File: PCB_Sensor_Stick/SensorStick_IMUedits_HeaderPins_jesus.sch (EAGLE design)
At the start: 50 parts

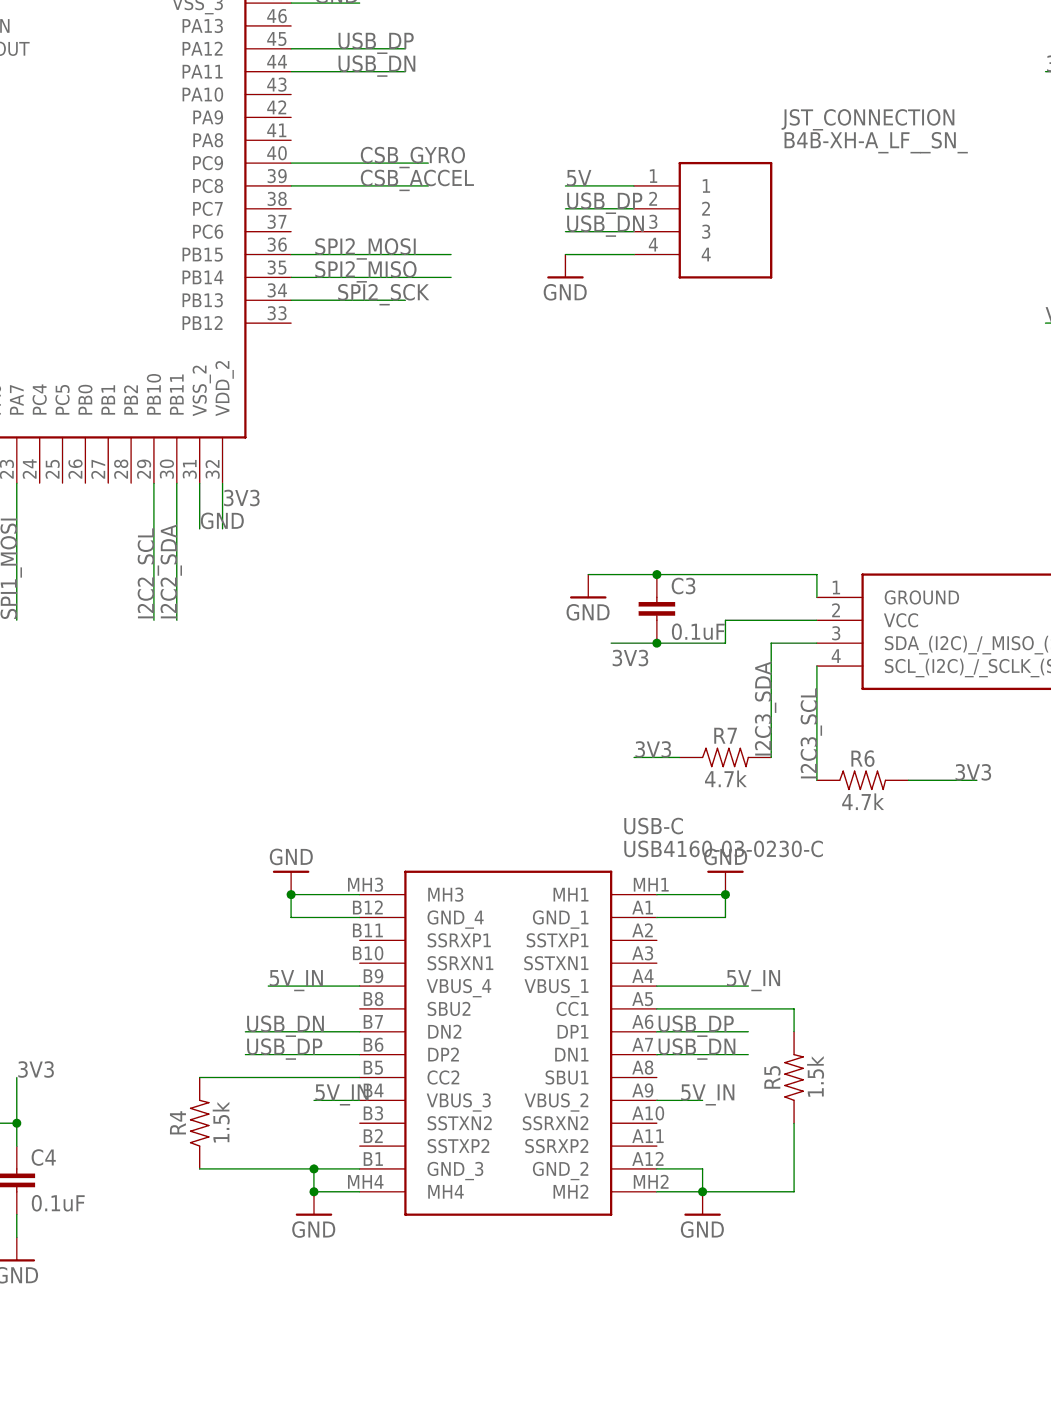
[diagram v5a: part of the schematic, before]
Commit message: J - Removed USB-C connector, wired JST-XH connector, PCB/Schematic first draft
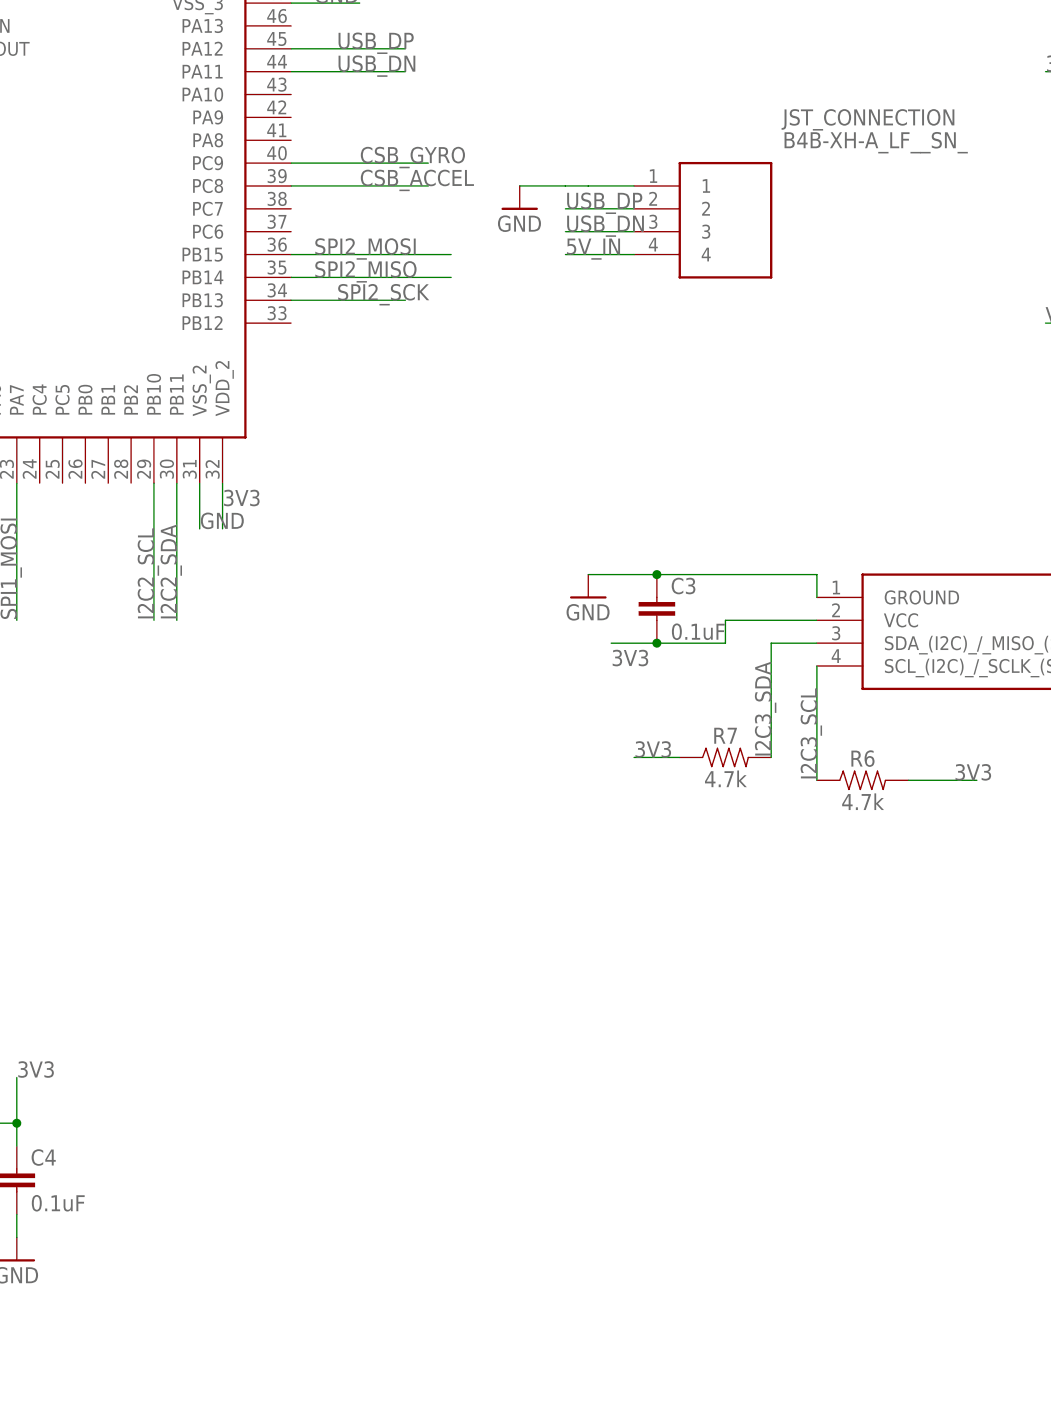
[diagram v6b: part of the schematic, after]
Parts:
- removed R4, R5: 1.5k, SparkFun-Resistors:1.5KOHM-0603-1/10W-1%
- removed USB-C: USB4160-03-0230-C, USB4160-03-0230-C:USB4160-03-0230-C
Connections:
- removed net N$10: R4.2, USB-C.CC2
- removed net N$3: R5.2, USB-C.CC1
- net 5V: no longer JST_CONNECTION.1
- net 5V_IN: now also JST_CONNECTION.4; no longer USB-C.VBUS_1, USB-C.VBUS_2, USB-C.VBUS_3, USB-C.VBUS_4
- net GND: now also JST_CONNECTION.1; no longer JST_CONNECTION.4, R4.1, R5.1, USB-C.GND_1, USB-C.GND_2, USB-C.GND_3, USB-C.GND_4, USB-C.MH1, USB-C.MH2, USB-C.MH3, USB-C.MH4
- net USB_DN: no longer USB-C.DN1, USB-C.DN2
- net USB_DP: no longer USB-C.DP1, USB-C.DP2
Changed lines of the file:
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@@
 <part name="C13" library="SparkFun-Capacitors" deviceset="0.22UF" device="-0603-25V-10%" value="0.22uF"/>
 <part name="GND14" library="supply1" library_urn="urn:adsk.eagle:library:371" deviceset="GND" device=""/>
-<part name="USB-C" library="USB4160-03-0230-C" deviceset="USB4160-03-0230-C" device=""/>
-<part name="GND15" library="supply1" library_urn="urn:adsk.eagle:library:371" deviceset="GND" device=""/>
-<part name="GND16" library="supply1" library_urn="urn:adsk.eagle:library:371" deviceset="GND" device=""/>
-<part name="GND17" library="supply1" library_urn="urn:adsk.eagle:library:371" deviceset="GND" device=""/>
-<part name="GND18" library="supply1" library_urn="urn:adsk.eagle:library:371" deviceset="GND" device=""/>
-<part name="R4" library="SparkFun-Resistors" deviceset="1.5KOHM" device="-0603-1/10W-1%" value="1.5k"/>
-<part name="R5" library="SparkFun-Resistors" deviceset="1.5KOHM" device="-0603-1/10W-1%" value="1.5k"/>
 <part name="L1" library="rcl" library_urn="urn:adsk.eagle:library:334" deviceset="L-US" device="L4035M" package3d_urn="urn:adsk.eagle:package:23478/2"/>
 <part name="C14" library="SparkFun-Capacitors" library_urn="urn:adsk.eagle:library:510" deviceset="0.1UF" device="-0603-25V-5%" package3d_urn="urn:adsk.eagle:package:37414/1" value="0.1uF"/>
@@
 <part name="JP1" library="pinhead" library_urn="urn:adsk.eagle:library:325" deviceset="PINHD-2X2" device="" package3d_urn="urn:adsk.eagle:package:22455/2"/>
 <part name="JST_CONNECTION" library="B4B-XH-A_LF__SN_" deviceset="B4B-XH-A_LF__SN_" device=""/>
-<part name="GND19" library="supply1" library_urn="urn:adsk.eagle:library:371" deviceset="GND" device=""/>
+<part name="GND15" library="supply1" library_urn="urn:adsk.eagle:library:371" deviceset="GND" device=""/>
 </parts>
 <sheets>
@@
 <attribute name="VALUE" x="91.44" y="101.6" size="1.778" layer="96"/>
 </instance>
-<instance part="USB-C" gate="G$1" x="152.4" y="-40.64" smashed="yes">
-<attribute name="NAME" x="181.61" y="-33.02" size="1.778" layer="95" align="center-left"/>
-<attribute name="VALUE" x="181.61" y="-35.56" size="1.778" layer="96" align="center-left"/>
-</instance>
-<instance part="GND15" gate="1" x="144.78" y="-38.1" smashed="yes" rot="R180">
-<attribute name="VALUE" x="147.32" y="-35.56" size="1.778" layer="96" rot="R180"/>
-</instance>
-<instance part="GND16" gate="1" x="193.04" y="-38.1" smashed="yes" rot="R180">
-<attribute name="VALUE" x="195.58" y="-35.56" size="1.778" layer="96" rot="R180"/>
-</instance>
-<instance part="GND17" gate="1" x="147.32" y="-76.2" smashed="yes">
-<attribute name="VALUE" x="144.78" y="-78.74" size="1.778" layer="96"/>
-</instance>
-<instance part="GND18" gate="1" x="190.5" y="-76.2" smashed="yes">
-<attribute name="VALUE" x="187.96" y="-78.74" size="1.778" layer="96"/>
-</instance>
-<instance part="R4" gate="G$1" x="134.62" y="-66.04" smashed="yes" rot="R90">
-<attribute name="NAME" x="133.096" y="-66.04" size="1.778" layer="95" font="vector" rot="R90" align="bottom-center"/>
-<attribute name="VALUE" x="136.144" y="-66.04" size="1.778" layer="96" font="vector" rot="R90" align="top-center"/>
-</instance>
-<instance part="R5" gate="G$1" x="200.66" y="-60.96" smashed="yes" rot="R90">
-<attribute name="NAME" x="199.136" y="-60.96" size="1.778" layer="95" font="vector" rot="R90" align="bottom-center"/>
-<attribute name="VALUE" x="202.184" y="-60.96" size="1.778" layer="96" font="vector" rot="R90" align="top-center"/>
-</instance>
 <instance part="L1" gate="G$1" x="233.68" y="38.1" smashed="yes" rot="R180">
 <attribute name="NAME" x="234.95" y="43.18" size="1.778" layer="95"/>
@@
 <attribute name="VALUE" x="199.39" y="43.18" size="1.778" layer="96" align="center-left"/>
 </instance>
-<instance part="GND19" gate="1" x="175.26" y="27.94" smashed="yes">
-<attribute name="VALUE" x="172.72" y="25.4" size="1.778" layer="96"/>
+<instance part="GND15" gate="1" x="170.18" y="35.56" smashed="yes">
+<attribute name="VALUE" x="167.64" y="33.02" size="1.778" layer="96"/>
 </instance>
 </instances>
@@
 </segment>
 <segment>
-<pinref part="USB-C" gate="G$1" pin="GND_4"/>
-<wire x1="152.4" y1="-43.18" x2="144.78" y2="-43.18" width="0.1524" layer="91"/>
-<wire x1="144.78" y1="-43.18" x2="144.78" y2="-40.64" width="0.1524" layer="91"/>
-<pinref part="USB-C" gate="G$1" pin="MH3"/>
-<wire x1="144.78" y1="-40.64" x2="152.4" y2="-40.64" width="0.1524" layer="91"/>
-<pinref part="GND15" gate="1" pin="GND"/>
-<junction x="144.78" y="-40.64"/>
-</segment>
-<segment>
-<pinref part="USB-C" gate="G$1" pin="GND_1"/>
-<wire x1="185.42" y1="-43.18" x2="193.04" y2="-43.18" width="0.1524" layer="91"/>
-<wire x1="193.04" y1="-43.18" x2="193.04" y2="-40.64" width="0.1524" layer="91"/>
-<pinref part="USB-C" gate="G$1" pin="MH1"/>
-<wire x1="193.04" y1="-40.64" x2="185.42" y2="-40.64" width="0.1524" layer="91"/>
-<pinref part="GND16" gate="1" pin="GND"/>
-<junction x="193.04" y="-40.64"/>
-</segment>
-<segment>
-<pinref part="USB-C" gate="G$1" pin="MH4"/>
-<wire x1="152.4" y1="-73.66" x2="147.32" y2="-73.66" width="0.1524" layer="91"/>
-<wire x1="147.32" y1="-73.66" x2="147.32" y2="-71.12" width="0.1524" layer="91"/>
-<pinref part="USB-C" gate="G$1" pin="GND_3"/>
-<wire x1="147.32" y1="-71.12" x2="152.4" y2="-71.12" width="0.1524" layer="91"/>
-<pinref part="GND17" gate="1" pin="GND"/>
-<junction x="147.32" y="-73.66"/>
-<wire x1="134.62" y1="-71.12" x2="147.32" y2="-71.12" width="0.1524" layer="91"/>
-<junction x="147.32" y="-71.12"/>
-<pinref part="R4" gate="G$1" pin="1"/>
-</segment>
-<segment>
-<pinref part="USB-C" gate="G$1" pin="MH2"/>
-<wire x1="185.42" y1="-73.66" x2="190.5" y2="-73.66" width="0.1524" layer="91"/>
-<wire x1="190.5" y1="-73.66" x2="190.5" y2="-71.12" width="0.1524" layer="91"/>
-<pinref part="USB-C" gate="G$1" pin="GND_2"/>
-<wire x1="190.5" y1="-71.12" x2="185.42" y2="-71.12" width="0.1524" layer="91"/>
-<pinref part="GND18" gate="1" pin="GND"/>
-<junction x="190.5" y="-73.66"/>
-<wire x1="190.5" y1="-73.66" x2="200.66" y2="-73.66" width="0.1524" layer="91"/>
-<pinref part="R5" gate="G$1" pin="1"/>
-<wire x1="200.66" y1="-66.04" x2="200.66" y2="-73.66" width="0.1524" layer="91"/>
-</segment>
-<segment>
 <pinref part="IMU" gate="G$1" pin="GNDA"/>
 <wire x1="93.98" y1="-68.58" x2="104.14" y2="-68.58" width="0.1524" layer="91"/>
@@
 </segment>
 <segment>
-<pinref part="JST_CONNECTION" gate="G$1" pin="4"/>
-<wire x1="182.88" y1="30.48" x2="175.26" y2="30.48" width="0.1524" layer="91"/>
-<pinref part="GND19" gate="1" pin="GND"/>
+<pinref part="JST_CONNECTION" gate="G$1" pin="1"/>
+<wire x1="182.88" y1="38.1" x2="177.8" y2="38.1" width="0.1524" layer="91"/>
+<pinref part="GND15" gate="1" pin="GND"/>
+<wire x1="177.8" y1="38.1" x2="175.26" y2="38.1" width="0.1524" layer="91"/>
+<wire x1="170.18" y1="38.1" x2="175.26" y2="38.1" width="0.1524" layer="91"/>
 </segment>
 </net>
@@
 <wire x1="144.78" y1="53.34" x2="157.48" y2="53.34" width="0.1524" layer="91"/>
 <label x="149.86" y="53.34" size="1.778" layer="95"/>
-</segment>
-<segment>
-<pinref part="USB-C" gate="G$1" pin="DP2"/>
-<wire x1="152.4" y1="-58.42" x2="139.7" y2="-58.42" width="0.1524" layer="91"/>
-<label x="139.7" y="-58.42" size="1.778" layer="95"/>
-</segment>
-<segment>
-<pinref part="USB-C" gate="G$1" pin="DP1"/>
-<wire x1="185.42" y1="-55.88" x2="195.58" y2="-55.88" width="0.1524" layer="91"/>
-<label x="185.42" y="-55.88" size="1.778" layer="95"/>
 </segment>
 <segment>
@@
 <label x="-33.02" y="5.08" size="1.778" layer="95"/>
 </segment>
-<segment>
-<pinref part="JST_CONNECTION" gate="G$1" pin="1"/>
-<wire x1="182.88" y1="38.1" x2="175.26" y2="38.1" width="0.1524" layer="91"/>
-<label x="175.26" y="38.1" size="1.778" layer="95"/>
-</segment>
 </net>
 <net name="5V_IN" class="0">
@@
 </segment>
 <segment>
-<pinref part="USB-C" gate="G$1" pin="VBUS_4"/>
-<wire x1="152.4" y1="-50.8" x2="142.24" y2="-50.8" width="0.1524" layer="91"/>
-<label x="142.24" y="-50.8" size="1.778" layer="95"/>
-</segment>
-<segment>
-<pinref part="USB-C" gate="G$1" pin="VBUS_1"/>
-<wire x1="185.42" y1="-50.8" x2="195.58" y2="-50.8" width="0.1524" layer="91"/>
-<label x="193.04" y="-50.8" size="1.778" layer="95"/>
-</segment>
-<segment>
-<pinref part="USB-C" gate="G$1" pin="VBUS_3"/>
-<wire x1="152.4" y1="-63.5" x2="147.32" y2="-63.5" width="0.1524" layer="91"/>
-<label x="147.32" y="-63.5" size="1.778" layer="95"/>
-</segment>
-<segment>
-<pinref part="USB-C" gate="G$1" pin="VBUS_2"/>
-<wire x1="185.42" y1="-63.5" x2="190.5" y2="-63.5" width="0.1524" layer="91"/>
-<label x="187.96" y="-63.5" size="1.778" layer="95"/>
+<pinref part="JST_CONNECTION" gate="G$1" pin="4"/>
+<wire x1="182.88" y1="30.48" x2="175.26" y2="30.48" width="0.1524" layer="91"/>
+<label x="175.26" y="30.48" size="1.778" layer="95"/>
 </segment>
 </net>
@@
 </segment>
 </net>
-<net name="N$10" class="0">
-<segment>
-<pinref part="USB-C" gate="G$1" pin="CC2"/>
-<wire x1="152.4" y1="-60.96" x2="134.62" y2="-60.96" width="0.1524" layer="91"/>
-<pinref part="R4" gate="G$1" pin="2"/>
-</segment>
-</net>
-<net name="N$3" class="0">
-<segment>
-<pinref part="USB-C" gate="G$1" pin="CC1"/>
-<wire x1="185.42" y1="-53.34" x2="200.66" y2="-53.34" width="0.1524" layer="91"/>
-<pinref part="R5" gate="G$1" pin="2"/>
-<wire x1="200.66" y1="-53.34" x2="200.66" y2="-55.88" width="0.1524" layer="91"/>
-</segment>
-</net>
 <net name="USB_DN" class="0">
 <segment>
-<pinref part="USB-C" gate="G$1" pin="DN2"/>
-<wire x1="152.4" y1="-55.88" x2="139.7" y2="-55.88" width="0.1524" layer="91"/>
-<label x="139.7" y="-55.88" size="1.778" layer="95"/>
-</segment>
-<segment>
-<pinref part="USB-C" gate="G$1" pin="DN1"/>
-<wire x1="185.42" y1="-58.42" x2="195.58" y2="-58.42" width="0.1524" layer="91"/>
-<label x="185.42" y="-58.42" size="1.778" layer="95"/>
-</segment>
-<segment>
 <pinref part="MICROCONTROLLER" gate="G$1" pin="PA11"/>

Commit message: J - Updates based off of Phil feedback
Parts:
- added JP6: (no value), pinhead:PINHD-1X6
- added R10: 0, SparkFun-Resistors:0OHM-0603-1/10W-5%
- added R5: 10k, SparkFun-Resistors:10KOHM-0603-1/10W-1%
- added S1: LL3301FF065QJ, ce-capstone:LL3301FF065QJ
- added U1: ECMF02-4CMX8, ECMF02-4CMX8:ECMF02-4CMX8
- added U2: TPD6F003DQDR, TPD6F003DQDR:TPD6F003DQDR
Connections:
- removed net N$6: C10.1, MAGNETOMETER.VDD_IO
- new net BOOT0: MICROCONTROLLER.PH3-BOOT0, R5.1, S1.3, S1.4
- new net DN: JST_CONNECTION.3, U1.D-_2
- new net DP: JST_CONNECTION.2, U1.D+_2
- new net NRST: GPS.RESET_N, MICROCONTROLLER.NRST, POWER_MODULE.PG, U2.CH4_IN
- new net NRST_O: JP6.4, U2.CH4_OUT
- new net RX_O: JP6.5, U2.CH5_OUT
- new net SWCLK: MICROCONTROLLER.PA14, U2.CH2_IN
- new net SWCLK_O: JP6.2, U2.CH2_OUT
- new net SWDIO: MICROCONTROLLER.PA13, U2.CH3_IN
- new net SWDIO_O: JP6.3, U2.CH3_OUT
- new net SWO: MICROCONTROLLER.PB3, U2.CH1_IN
- new net SWO_O: JP6.1, U2.CH1_OUT
- new net TX_O: JP6.6, U2.CH6_OUT
- net 3V3: now also BAROMETER.CSB, BAROMETER.SDO, C10.1, GPS.V_BCKP, MAGNETOMETER.CS, MAGNETOMETER.VDD_IO, S1.1, S1.2, U1.VBUS
- net GND: now also R5.2, U1.GND, U1.GND_2, U2.EPAD; no longer MAGNETOMETER.CS
- net GPIO_EXTI2: now also R10.1
- net GPIO_EXTI4: now also IMU.INT2, R10.2; no longer BAROMETER.SDO
- net USART3_RX: now also U2.CH5_IN
- net USART3_TX: now also U2.CH6_IN
- net USB_DN: now also U1.D-; no longer JST_CONNECTION.3
- net USB_DP: now also U1.D+; no longer JST_CONNECTION.2

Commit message: J - Current version with various changes according the feedback
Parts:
- added C23: 0.1uF, SparkFun-Capacitors:0.1UF-0603-25V-5%
- added C24, C25, C26: 1.0uF, SparkFun-Capacitors:1.0UF-0402-16V-10%
- added R4: 10k, SparkFun-Resistors:10KOHM-0603-1/10W-1%
- added S2: LL3301FF065QJ, ce-capstone:LL3301FF065QJ
- added USB_COMM_MODE_FILTER: ECMF02-4CMX8, ECMF02-4CMX8:ECMF02-4CMX8
- added Y1: ECS-TXO-3225MV-400-TR, SamacSys_Parts:ECS-TXO-3225MV-400-TR
- U1: value ECMF02-4CMX8 -> LT1461CIS8-3PBF; device ECMF02-4CMX8:ECMF02-4CMX8 -> LT1461:LT1461CIS8-3PBF
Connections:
- new net GPS_MEM: GPS.SAFEBOOT_N
- new net N$1: MICROCONTROLLER.PH0-OSC_IN
- new net N$10: AIRSPEED.VCC, C25.1, C26.1, C3.2, U1.VOUT
- new net N$3: MICROCONTROLLER.PH1-OSC_OUT
- new net N$4: Y1.OUTPUT
- new net N$6: C24.1, U1.VIN
- net 3V3: now also R4.2, USB_COMM_MODE_FILTER.VBUS, Y1.VDD; no longer AIRSPEED.VCC, C3.2, U1.VBUS
- net DN: now also USB_COMM_MODE_FILTER.D-_2; no longer U1.D-_2
- net DP: now also USB_COMM_MODE_FILTER.D+_2; no longer U1.D+_2
- net GND: now also C23.2, C24.2, C25.2, C26.2, S2.3, S2.4, USB_COMM_MODE_FILTER.GND, USB_COMM_MODE_FILTER.GND_2, Y1.GROUND; no longer U1.GND_2
- net GPIO_EXTI0: no longer JP2.3
- net GPIO_EXTI4: now also JP2.3
- net NRST: now also C23.1, R4.1, S2.1, S2.2
- net USB_DN: now also USB_COMM_MODE_FILTER.D-; no longer U1.D-
- net USB_DP: now also USB_COMM_MODE_FILTER.D+; no longer U1.D+
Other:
- moved on the sheet: AIRSPEED, BAROMETER, C1, C2, C3, C4, C5, C6, C7, C8, C9, D1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
